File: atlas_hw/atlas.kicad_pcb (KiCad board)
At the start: 4 copper layers, 140.3 x 99.9 mm, 180 parts, among them J1 USB_C_Receptacle_USB2.0, J10 PSP_LCD, J11 UART3_EXT, J12 IO_EXT, J13 IO_MAIN, J2 DEBUG_STM, J3 PSP_TOUCH, J4 UPDI_DSS, J5 CELL_THERM, J6 LPM027M128B, J7 FLEX_12380-03, J8 Micro_SD_Card_Det, J9 PSP_LCD_BL, Q1 Q_NMOS_DGS, Q2 Q_NMOS_DGS, Q4 Q_NMOS_DGS, Q5 Q_NMOS_DGS, SW1 BTN_L_EXT, SW2 BTN_0_EXT, SW3 ResetSTM, SW4 BTN_R_EXT, SW5 BTN_PWR_EXT, U1 STM32H723VITx, U10 BQ25611D, U11 L96-M33, U13 LSF0108, U14 NPP600SNADJ, U15 TPS61073, U16 PAM2841, U2 S27KL0641DABHV023, U3 MCP1811B, U4 TLV62569DBV, U5 MX25L3233FM2I-08G, U6 LC709203F, U7 ATtiny402-SS, U8 MS5637, U9 MC6470, Y1 16M, Y4 32k

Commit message: passive placement
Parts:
- removed C55: 0.1u, Capacitor_SMD:C_0402_1005Metric
- removed R2, R80, R81: 0, Resistor_SMD:R_0402_1005Metric
- removed R46: 0, Resistor_SMD:R_0612_1632Metric
- added C20: 1u, Capacitor_SMD:C_0603_1608Metric, B.Cu at (206.1, 107.2)
- added C28: 0.1u, Capacitor_SMD:C_0402_1005Metric, B.Cu at (211.5, 112.5)
- C18, C19, C21, C22, C26, C5, C51, C53, C54, C56, C57, C6, C61, C9, R12, R13, R14, R15, R21, R22, R23, R26, R27, R30, R31, R32, R33, R35, R36, R39, R41, R82, R83, R84, R86: moved to B.Cu
- J11: footprint Connector_PinHeader_1.00mm:PinHeader_1x06_P1.00mm_Vertical -> Connector_PinHeader_1.00mm:PinHeader_1x06_P1.00mm_Vertical_SMD_Pin1Left
- J7, R37: moved to F.Cu
- R1, R25: value 10k -> 100k
- R44, R6: value 10k -> 100k; moved to B.Cu
- moved C51 242.5 mm to (208.6, 89.8), turned to 90 degrees
- moved C9 234.7 mm to (182.3, 94.4), turned to 90 degrees
- moved R86 224.2 mm to (214.2, 112.5), turned to 90 degrees
- moved C21 219.2 mm to (186.4, 107.0), turned to 45 degrees
- moved R55 214.3 mm to (195.3, 102.9), turned to 180 degrees
- moved C19 209.6 mm to (185.1, 108.3), turned to 225 degrees
- moved R82 209.0 mm to (206.8, 86.9), turned to 270 degrees
- moved R30 207.3 mm to (202.6, 130.3)
- moved C54 204.2 mm to (206.6, 106.0)
- moved C57 199.9 mm to (183.2, 127.3), turned to 90 degrees
- moved C2 196.7 mm to (190.0, 93.8), turned to 180 degrees
- moved R23 196.3 mm to (202.6, 133.3)
- moved R6 195.5 mm to (212.8, 112.5), turned to 90 degrees
- moved C27 195.3 mm to (205.8, 133.7), turned to 270 degrees
- moved R83 193.4 mm to (205.8, 86.9), turned to 270 degrees
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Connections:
- C48 pad 2: Net-(C48-Pad2) -> /VCC_SYS
- C51 pad 1: Net-(C51-Pad1) -> /VCC_LCD_PWR
- C53 pad 1: Net-(C51-Pad1) -> /VCC_LCD_PWR
- C54 pad 1: Net-(C54-Pad1) -> /VCC_MCU_3V3
- J10 pad 3: Net-(C54-Pad1) -> /VCC_MCU_3V3
- J10 pad 35: Net-(C51-Pad1) -> /VCC_LCD_PWR
- J10 pad 36: Net-(C51-Pad1) -> /VCC_LCD_PWR
- J10 pad 4: Net-(C54-Pad1) -> /VCC_MCU_3V3
- J11 pad 3: /USART3_RX_NCP -> /USART3_CTS_NCP
- J11 pad 4: /USART3_TX_NCP -> /USART3_RTS_NCP
- J11 pad 5: /USART3_CTS_NCP -> /USART3_TX_NCP
- J11 pad 6: /USART3_RTS_NCP -> /USART3_RX_NCP
- L10 pad 1: Net-(C48-Pad2) -> /VCC_SYS
- R1 pad 1: /VCC_BACKUP -> /VCC_MCU_3V3
- U1 pad 19: Net-(R2-Pad1) -> GND
- U13 pad 1: /VDD_SD_IO_3V3_1V8 -> GND
- U13 pad 10: /SDMMC1_D1 -> GND
- U13 pad 11: /SD_D1 -> GND
- U13 pad 12: /SD_D0 -> /SD_D2
- U13 pad 13: /SD_CLK -> /SD_D3
- U13 pad 14: /SD_CLK -> /SD_CMD
- U13 pad 15: /SD_CMD -> /SD_CLK
- U13 pad 16: /SD_D3 -> /SD_CLK
- U13 pad 17: /SD_D2 -> /SD_D0
- U13 pad 18: GND -> /SD_D1
- U13 pad 19: GND -> /VDD_SD_IO_3V3_1V8
- U13 pad 2: Net-(R43-Pad2) -> /VCC_MCU_3V3
- U13 pad 20: /VCC_MCU_3V3 -> Net-(R43-Pad2)
- U13 pad 21: /VDD_SD_IO_3V3_1V8 -> GND
- U13 pad 3: GND -> /SDMMC1_D1
- U13 pad 4: /SDMMC1_D2 -> /SDMMC1_D0
- U13 pad 5: /SDMMC1_D3 -> /SDMMC1_CKIN
- U13 pad 6: /SDMMC1_CMD -> /SDMMC1_CK
- U13 pad 7: /SDMMC1_CK -> /SDMMC1_CMD
- U13 pad 8: /SDMMC1_CKIN -> /SDMMC1_D3
- U13 pad 9: /SDMMC1_D0 -> /SDMMC1_D2
- U16 pad 2: Net-(C48-Pad2) -> /VCC_SYS
- U9 pad 10: (no net) -> Net-(U9-Pad10)
- Y1 pad 1: /RCC_OSC_IN -> /RCC_OSC_OUT
- Y1 pad 2: /RCC_OSC_OUT -> /RCC_OSC_IN
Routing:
- net /LTDC_VS: track 36.7 -> 4.70 mm
- net GND: track 34.9 -> 19.7 mm, vias 1 -> 0
- net /USB_PORT_VBUS: track 0.75 -> 16.0 mm
- net /GPS_3DF: track 0.00 -> 12.5 mm, vias 0 -> 1
- net /USART3_RTS_NCP: track 0.00 -> 12.0 mm
- net /USART3_RX_NCP: track 0.00 -> 11.4 mm
- net /CHG_STAT: track 1.21 -> 12.4 mm, vias 1 -> 2
- net /USART3_CTS_NCP: track 0.00 -> 10.7 mm
- net /SDMMC1_D1: track 0.00 -> 10.7 mm, vias 0 -> 1
- net /USART3_TX_NCP: track 0.00 -> 9.62 mm
- net /SDMMC1_D2: track 14.4 -> 5.60 mm, vias 1 -> 0
- net Net-(C48-Pad2): track 6.68 -> 0.00 mm
- net /VCC_SYS: track 7.19 -> 13.9 mm
- net /SDMMC1_D3: track 11.7 -> 5.08 mm
- net /SDMMC1_CKIN: track 5.08 -> 11.7 mm
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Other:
- board size 140.3 x 99.9 mm -> 60.5 x 77.4 mm

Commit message: filling out layout
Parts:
- removed R23, R30: 0, Resistor_SMD:R_0402_1005Metric
- C58: moved to B.Cu
- moved D2 52.6 mm to (182.0, 86.8)
- moved R10 49.6 mm to (182.0, 89.9)
- moved R36 7.59 mm to (196.6, 124.6)
- moved C58 1.41 mm to (177.6, 125.0), turned to 90 degrees
- moved R1 1.04 mm to (190.4, 125.2), turned to 45 degrees
- moved R49 0.96 mm to (196.1, 121.1), turned to 180 degrees
- moved R12 0.80 mm to (207.1, 133.0)
- moved R34 0.50 mm to (192.9, 103.9)
- moved C57 0.40 mm to (183.6, 127.3)
- moved C8 0.17 mm to (210.5, 109.7)
- moved R38 0.10 mm to (195.2, 103.9)
- moved R55 0.10 mm to (195.2, 102.9)
- moved C34 0.10 mm to (192.9, 102.9)
- moved J7 0.08 mm to (196.6, 122.8)
- turned R9 to 90 degrees
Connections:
- J13 pad 2: /SW_L -> /STM_STATUS_L
- J13 pad 3: /STM_STATUS_L -> /STM_STATUS_0
- J13 pad 4: /SW_0 -> /STM_STATUS_R
- J13 pad 5: /STM_STATUS_0 -> /SW_PWR
- J13 pad 7: /STM_STATUS_R -> /SW_0
- J13 pad 8: /SW_PWR -> /SW_L
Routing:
- net /VCC_BACKUP: track 0.00 -> 81.6 mm, vias 0 -> 5
- net /VCC_SYS: track 13.9 -> 88.1 mm, vias 0 -> 6
- net /VCC_MCU_3V3: track 7.54 -> 77.4 mm, vias 0 -> 20
- net GND: track 19.7 -> 77.9 mm, vias 0 -> 54
- net /SW_PWR: track 0.00 -> 44.6 mm, vias 0 -> 1
- net /USB_PORT_VBUS: track 16.0 -> 56.6 mm, vias 0 -> 2
- net /I2C4_SDA_SYSTEM: track 1.31 -> 40.8 mm, vias 1 -> 3
- net /PWR_ACK_DSS: track 0.00 -> 37.3 mm, vias 0 -> 2
- net /I2C4_SCL_SYSTEM: track 1.25 -> 37.4 mm, vias 1 -> 3
- net /PWR_SW_DSS: track 0.00 -> 35.3 mm, vias 0 -> 2
- net /DEBUG_SWDIO_STM: track 0.00 -> 31.2 mm, vias 0 -> 2
- net /DEBUG_SWDCLK_STM: track 0.00 -> 29.6 mm, vias 0 -> 2
- net /USB_STM_D+: track 0.00 -> 29.5 mm, vias 0 -> 1
- net /T3C1_LCD_BL: track 0.00 -> 27.9 mm, vias 0 -> 3
- net /USB_STM_D-: track 0.00 -> 27.5 mm, vias 0 -> 1
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- added copper zone on In1.Cu, net /VCC_MCU_3V3
- added copper zone on B.Cu, net GND
- added copper zone on F.Cu, net GND
- added copper zone on In2.Cu, net GND

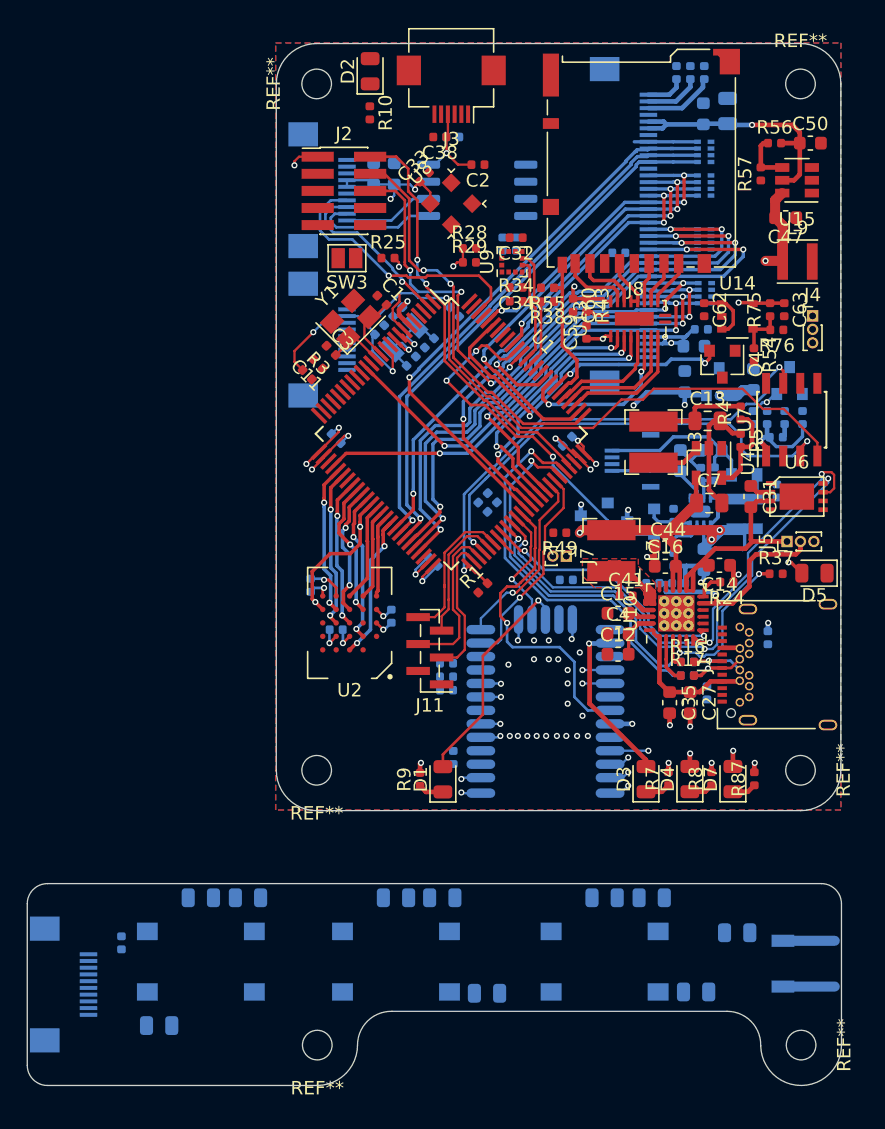
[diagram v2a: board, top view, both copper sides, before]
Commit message: layout mostly done, split btn into diffrent file
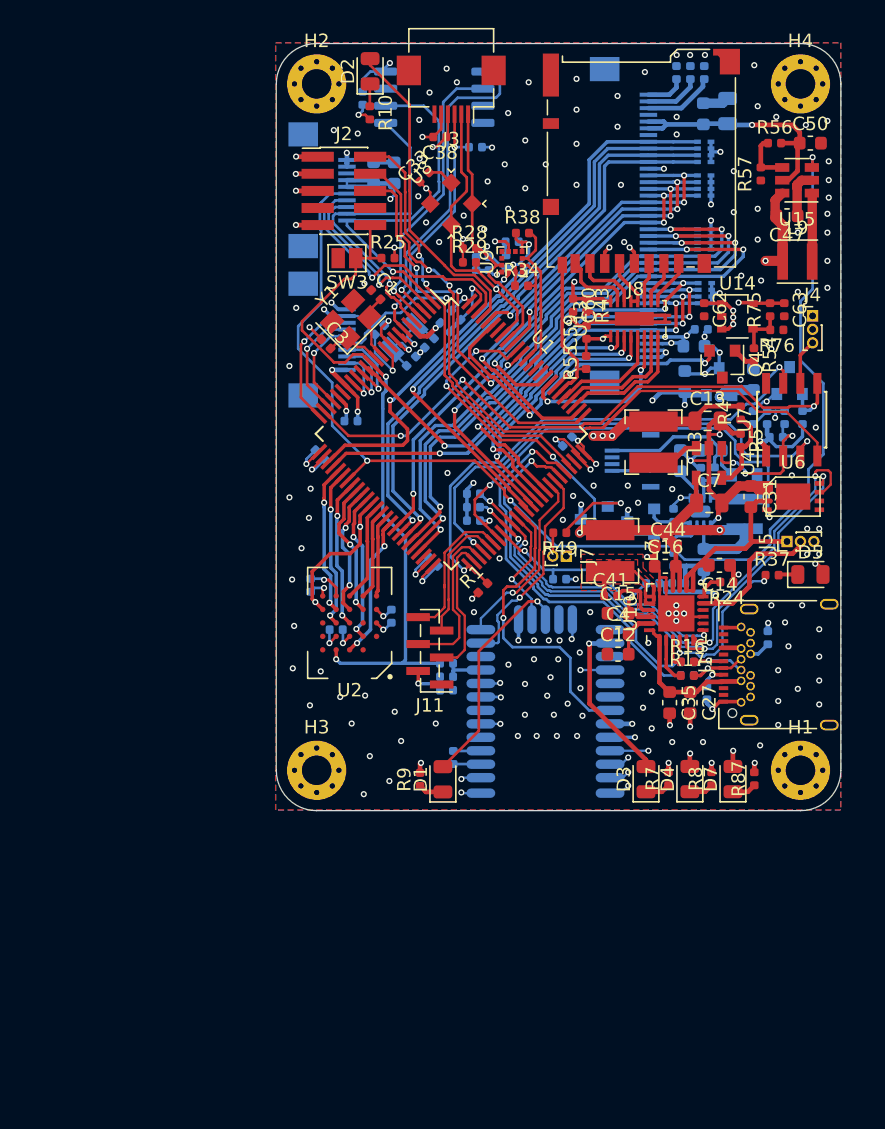
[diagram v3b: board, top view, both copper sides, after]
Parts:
- removed C17, C61: 0.1u, Capacitor_SMD:C_0402_1005Metric
- removed D10: STM_STATUS_R, LED_SMD:LED_0805_2012Metric
- removed D8: STM_STATUS_L, LED_SMD:LED_0805_2012Metric
- removed D9: STM_STATUS_0, LED_SMD:LED_0805_2012Metric
- removed J12: IO_EXT, Connector_FFC-FPC:Hirose_FH12-10S-0.5SH_1x10-1MP_P0.50mm_Horizontal
- removed R11, R18, R19: 1k, Resistor_SMD:R_0805_2012Metric
- removed R3: 0, Resistor_SMD:R_0402_1005Metric
- removed R40, R45, R48, R50: 100k, Resistor_SMD:R_0805_2012Metric
- removed REF** (x6): MountingHole_2.2mm_M2, MountingHole:MountingHole_2.2mm_M2
- removed SW1: BTN_L_EXT, Button_Switch_SMD:SW_SPST_B3S-1000
- removed SW2: BTN_0_EXT, Button_Switch_SMD:SW_SPST_B3S-1000
- removed SW4: BTN_R_EXT, Button_Switch_SMD:SW_SPST_B3S-1000
- removed SW5: BTN_PWR_EXT, Button_Switch_SMD:SW_SPST_B3U-1000P
- added H1: MountingHole_Pad, MountingHole:MountingHole_2.2mm_M2_Pad_Via, F.Cu at (214.0, 138.8)
- added H2: MountingHole_Pad, MountingHole:MountingHole_2.2mm_M2_Pad_Via, F.Cu at (178.1, 87.8)
- added H3: MountingHole_Pad, MountingHole:MountingHole_2.2mm_M2_Pad_Via, F.Cu at (178.1, 138.8)
- added H4: MountingHole_Pad, MountingHole:MountingHole_2.2mm_M2_Pad_Via, F.Cu at (214.0, 87.8)
- C11, C2, C32, C34: moved to B.Cu
- U10: footprint Package_DFN_QFN:WQFN-24-1EP_4x4mm_P0.5mm_EP2.7x2.7mm_ThermalVias -> Package_DFN_QFN:WQFN-24-1EP_4x4mm_P0.5mm_EP2.7x2.7mm
- moved R41 22.7 mm to (189.7, 120.2), turned to 0 degrees
- moved C2 9.89 mm to (181.5, 88.8), turned to 90 degrees
- moved U5 7.61 mm to (186.8, 88.7)
- moved R55 6.25 mm to (198.1, 108.5), turned to 90 degrees
- moved R38 5.43 mm to (193.3, 98.8), turned to 0 degrees
- moved C11 4.90 mm to (180.6, 112.8), turned to 0 degrees
- moved C6 3.70 mm to (187.6, 105.8), turned to 315 degrees
- moved R26 3.31 mm to (189.9, 101.1)
- moved C34 2.04 mm to (192.1, 101.0), turned to 90 degrees
- moved R42 1.85 mm to (189.8, 92.5), turned to 180 degrees
- moved R27 1.78 mm to (190.8, 101.1)
- moved C24 1.70 mm to (178.3, 115.3)
- moved R35 1.57 mm to (189.7, 119.2), turned to 0 degrees
- moved R33 1.22 mm to (189.7, 118.2), turned to 0 degrees
- moved R34 1.22 mm to (193.3, 102.8)
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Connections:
- C11 pad 1: Net-(C11-Pad1) -> /VCC_MCU_3V3
- R35 pad 2: /I2C4_SDA_SYSTEM -> /I2C4_SCL_SYSTEM
- U1 pad 16: /STM_STATUS_L -> /STM_STATUS_R
- U1 pad 18: /STM_STATUS_R -> /STM_STATUS_L
- U1 pad 21: Net-(C11-Pad1) -> /VCC_MCU_3V3
- U1 pad 22: /SW_C -> /SW_R
- U1 pad 23: /SW_L -> /SW_0
- U1 pad 25: /SW_R -> /SW_L
- U5 pad 1: /SPI4_FLASH_CS -> /SPI4_FLASH_NCS
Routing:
- net GND: track 77.9 -> 173.9 mm, vias 54 -> 197
- net /EN_LCD_PWR: track 3.40 -> 95.8 mm, vias 0 -> 3
- net /DEBUG_NRESET_STM: track 0.00 -> 50.6 mm, vias 0 -> 2
- net /~USB_DET: track 0.00 -> 46.5 mm, vias 0 -> 3
- net /LTDC_VS: track 4.70 -> 42.9 mm, vias 0 -> 1
- net /LC709203_INT: track 1.59 -> 35.7 mm, vias 0 -> 3
- net /SPI4_FLASH_NCS: track 0.00 -> 24.4 mm, vias 0 -> 1
- net /STM_STATUS_B: track 0.00 -> 23.9 mm
- net /I2C1_SDA_SENSOR: track 0.00 -> 23.4 mm, vias 0 -> 2
- net /SPI4_MISO_APP: track 0.00 -> 21.6 mm, vias 0 -> 1
- net /I2C1_SCL_SENSOR: track 0.00 -> 20.8 mm
- net /SPI4_SCK_APP: track 6.73 -> 26.5 mm, vias 0 -> 1
- net /VCC_MCU_3V3: track 77.4 -> 95.8 mm, vias 20 -> 40
- net /STC911_INT: track 3.24 -> 20.9 mm, vias 0 -> 2
- net /SPI4_MOSI_APP: track 9.40 -> 23.9 mm, vias 0 -> 1
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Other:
- board size 60.5 x 77.4 mm -> 41.9 x 57 mm

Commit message: atlas dev simplifcations
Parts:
- removed C31, C35, C47, C50: 1u, Capacitor_SMD:C_0603_1608Metric
- removed C33: 0.1u, Capacitor_SMD:C_0402_1005Metric
- removed C41: 47n, Capacitor_SMD:C_0402_1005Metric
- removed C44: 4.7u, Capacitor_SMD:C_0603_1608Metric
- removed D2: STM_STATUS_B, LED_SMD:LED_0805_2012Metric
- removed D5: CHARGE_STATUS, LED_SMD:LED_0805_2012Metric
- removed J11: UART3_EXT, Connector_PinHeader_1.00mm:PinHeader_1x06_P1.00mm_Vertical_SMD_Pin1Left
- removed J13: IO_MAIN, Connector_FFC-FPC:Hirose_FH12-10S-0.5SH_1x10-1MP_P0.50mm_Horizontal
- removed J7: FLEX_12380-03, Connector_PinHeader_1.00mm:PinHeader_1x02_P1.00mm_Vertical
- removed L7: 1u, Inductor_SMD:L_Bourns-SRN4018
- removed L9: L_Small, Inductor_SMD:L_Taiyo-Yuden_MD-3030
- removed Q5: Q_NMOS_DGS, Package_TO_SOT_SMD:SOT-23
- removed R33, R35: 4.7k, Resistor_SMD:R_0402_1005Metric
- removed R36, R41, R85, R86: 100k, Resistor_SMD:R_0402_1005Metric
- removed R37: 1k, Resistor_SMD:R_0402_1005Metric
- removed R49: 100, Resistor_SMD:R_0402_1005Metric
- removed R56, R57: NP, Resistor_SMD:R_0402_1005Metric
- removed U10: BQ25611D, Package_DFN_QFN:WQFN-24-1EP_4x4mm_P0.5mm_EP2.7x2.7mm
- removed U15: TPS61073, Package_TO_SOT_SMD:SOT-23-6
- removed U8: MS5637, atlas:QFN-4_3x3_Pitch2mm
- added C17: 0.1u, Capacitor_SMD:C_0402_1005Metric, F.Cu at (159.7, 112.0)
- added D10: STM_STATUS_R, LED_SMD:LED_0805_2012Metric, F.Cu at (150.8, 107.1)
- added D8: STM_STATUS_L, LED_SMD:LED_0805_2012Metric, F.Cu at (144.7, 112.6)
- added D9: STM_STATUS_0, LED_SMD:LED_0805_2012Metric, F.Cu at (139.5, 115.5)
- added L1: 2.2u, Inductor_SMD:L_Bourns-SRN4018, F.Cu at (145.5, 108.3)
- added R11: 1k, Resistor_SMD:R_0805_2012Metric, F.Cu at (153.5, 110.1)
- added R18: 1k, Resistor_SMD:R_0805_2012Metric, F.Cu at (148.3, 115.6)
- added R19: 1k, Resistor_SMD:R_0805_2012Metric, F.Cu at (164.6, 98.6)
- added R2: 100k, Resistor_SMD:R_0402_1005Metric, F.Cu at (156.8, 112.5)
- added R23: NP, Resistor_SMD:R_0402_1005Metric, F.Cu at (167.0, 108.0)
- added R3: 100k, Resistor_SMD:R_0402_1005Metric, F.Cu at (156.0, 115.0)
- added R30: NP, Resistor_SMD:R_0402_1005Metric, F.Cu at (162.6, 110.3)
- added R40: 100k, Resistor_SMD:R_0805_2012Metric, F.Cu at (155.7, 103.1)
- added R45: 100k, Resistor_SMD:R_0805_2012Metric, F.Cu at (160.2, 101.5)
- added R48: 100k, Resistor_SMD:R_0805_2012Metric, F.Cu at (155.2, 107.0)
- added R50: 100k, Resistor_SMD:R_0805_2012Metric, F.Cu at (149.1, 112.6)
- added SW1: BTN_L_EXT, Button_Switch_SMD:SW_SPST_B3S-1000, F.Cu at (148.0, 101.3)
- added SW2: BTN_0_EXT, Button_Switch_SMD:SW_SPST_B3S-1000, F.Cu at (136.9, 109.8)
- added SW4: BTN_R_EXT, Button_Switch_SMD:SW_SPST_B3S-1000, F.Cu at (136.9, 101.3)
- added SW5: BTN_PWR_EXT, Button_Switch_SMD:SW_SPST_B3U-1000P, F.Cu at (134.3, 116.2)
- C12, C14, C4: value 4.7u -> 1u
- C15: value 4.7u -> 10u; footprint Capacitor_SMD:C_0603_1608Metric -> Capacitor_SMD:C_0805_2012Metric
- C16: value 4.7u -> 0.1u; footprint Capacitor_SMD:C_0603_1608Metric -> Capacitor_SMD:C_0402_1005Metric
- C18: value 0.1u -> 10u; footprint Capacitor_SMD:C_0402_1005Metric -> Capacitor_SMD:C_0603_1608Metric; moved to F.Cu
- C5: value 0.1u -> 1u; moved to F.Cu
- C9: value 1u -> 10u; footprint Capacitor_SMD:C_0603_1608Metric -> Capacitor_SMD:C_0805_2012Metric; moved to F.Cu
- J1: value USB_C_Receptacle_USB2.0 -> USB_B_Micro; footprint Connector_USB:USB_C_Receptacle_Amphenol_12401548E4-2A -> Connector_USB:USB_Micro-B_Molex-105017-0001
- J5: value CELL_THERM -> EXP_L; footprint Connector_PinHeader_1.00mm:PinHeader_1x03_P1.00mm_Vertical -> Connector_PinHeader_2.54mm:PinHeader_1x18_P2.54mm_Vertical
- J6: value LPM027M128B -> EXP_R; footprint Connector_FFC-FPC:Hirose_FH12-10S-0.5SH_1x10-1MP_P0.50mm_Horizontal -> Connector_PinHeader_2.54mm:PinHeader_1x18_P2.54mm_Vertical; moved to F.Cu
- Q1: moved to F.Cu
- R10: value 1k -> 100k
- R12, R13: value 5.1k -> 0; moved to F.Cu
- R17, R24: value 0 -> NP
- R31, R32: value 100k -> NP; moved to F.Cu
- U6: value LC709203F -> ST1PS02; footprint atlas:WDFN-8_3x4mm_0.6mm_1.96x2.56mm -> atlas:TQFN-12_1.7x2.0mm_P0.4mm
- moved R13 56.8 mm to (156.0, 117.0), turned to 0 degrees
- moved C14 56.0 mm to (152.6, 115.3), turned to 0 degrees
- moved U6 55.2 mm to (159.9, 105.2), turned to 0 degrees
- moved J6 53.1 mm to (231.5, 92.6), turned to 0 degrees
- moved R12 52.1 mm to (161.2, 108.3), turned to 0 degrees
- moved C15 49.3 mm to (160.2, 98.6)
- moved R17 49.1 mm to (158.9, 116.5)
- moved Q1 47.7 mm to (155.8, 99.4), turned to 0 degrees
- moved R24 47.6 mm to (162.6, 112.3), turned to 0 degrees
- moved C4 46.7 mm to (157.8, 109.8)
- moved C12 46.2 mm to (164.4, 101.3)
- moved J1 45.4 mm to (238.8, 93.2), turned to 0 degrees
- moved R31 45.3 mm to (158.9, 114.5)
- moved R16 45.1 mm to (165.5, 110.0)
- moved R32 44.2 mm to (164.1, 108.0)
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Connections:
- C11 pad 1: /VCC_MCU_3V3 -> /VCC_3V3
- C12 pad 1: GND -> /VCAP2_STM
- C12 pad 2: Net-(C12-Pad2) -> GND
- C13 pad 1: /VCC_MCU_3V3 -> /VCC_3V3
- C14 pad 1: GND -> /VCAP2_STM
- C14 pad 2: /CELL_POS -> GND
- C15 pad 1: GND -> /VCC_CORE
- C15 pad 2: Net-(C15-Pad2) -> GND
- C16 pad 1: GND -> /VCAP2
- C16 pad 2: /VCC_SYS -> GND
- C18 pad 1: /VCC_MCU_3V3 -> /USB_PORT_VBUS
- C2 pad 2: /VCC_MCU_3V3 -> /VCC_3V3
- C22 pad 1: /VCC_MCU_3V3 -> /VCC_3V3
- C23 pad 1: /VCC_MCU_3V3 -> /VCC_3V3
- C24 pad 1: /VCC_MCU_3V3 -> /VCC_3V3
- C25 pad 1: /VCC_MCU_3V3 -> /VCC_3V3
- C26 pad 1: /VCC_MCU_3V3 -> /VCC_3V3
- C32 pad 1: /VCC_MCU_3V3 -> /VCC_3V3
- C34 pad 1: /VCC_MCU_3V3 -> /VCC_3V3
- C4 pad 1: GND -> /VCAP1_STM
- C4 pad 2: Net-(C12-Pad2) -> GND
- C5 pad 1: /VCC_MCU_3V3 -> /VCAP1_STM
- C51 pad 1: /VCC_LCD_PWR -> /VCC_SYS
- C53 pad 1: /VCC_LCD_PWR -> /VCC_SYS
- C56 pad 2: /VCC_MCU_3V3 -> /VCC_3V3
- C57 pad 2: /VCC_MCU_3V3 -> /VCC_3V3
- C58 pad 2: /VCC_MCU_3V3 -> /VCC_3V3
- C9 pad 1: /VCC_MCU_3V3 -> /VCC_SYS
- D4 pad 2: /VCC_MCU_3V3 -> /VCC_3V3
- J10 pad 35: /VCC_LCD_PWR -> /VCC_SYS
- J10 pad 36: /VCC_LCD_PWR -> /VCC_SYS
- J2 pad 1: /VCC_MCU_3V3 -> /VCC_3V3
- J5 pad 1: /CELL_POS -> /USB_PORT_VBUS
- J5 pad 2: /CELL_NTC -> /VCC_SYS
- J5 pad 3: GND -> /VCC_BACKUP
- J6 pad 1: /SPI4_SCK_APP -> GND
- J6 pad 10: GND -> /PE0
- J6 pad 2: /SPI4_MOSI_APP -> /SDMMC1_CKIN_PB8
- J6 pad 3: /SPI4_OPT_LCD_NCS -> /PB7
- J6 pad 4: /OPT_LCD_COM_INV -> /PB6
- J6 pad 5: /EN_LCD_PWR -> GND
- J6 pad 6: /VCC_MCU_3V3 -> /PD7
- J6 pad 7: /VCC_MCU_3V3 -> /PD6
- J6 pad 8: /EXTMODE -> /SDMMC1_VSEL_PD1
- J8 pad 9: /SDMMC1_DET -> /SD_DET
- L3 pad 2: /VCC_MCU_3V3 -> /VCC_3V3
- Q1 pad 1: Net-(Q1-Pad1) -> /VCORE_EN
- Q1 pad 2: /T3C1_LCD_BL -> /STM_VCORE_EN
- R10 pad 1: Net-(D2-Pad1) -> /STM_VCORE_GOOD
- R10 pad 2: GND -> /VCC_MCU_3V3
- R12 pad 1: GND -> /VCAP1
- R12 pad 2: Net-(J1-PadA5) -> /VCC_CORE
- R13 pad 1: Net-(J1-PadB5) -> /VCAP2
- R13 pad 2: GND -> /VCC_CORE
- R14 pad 1: /USB_STM_D- -> /USB_STM_D+
- R14 pad 2: /USB_PORT_D- -> /USB_PORT_D+
- R15 pad 1: /USB_STM_D+ -> /USB_STM_D-
- R15 pad 2: /USB_PORT_D+ -> /USB_PORT_D-
- R16 pad 1: /USB_CHGR_D- -> /VCC_SYS
- R16 pad 2: /USB_PORT_D- -> /USB_PORT_VBUS
- R17 pad 1: /USB_CHGR_D+ -> /SDMMC1_D2
- R17 pad 2: /USB_PORT_D+ -> /SD_D2
- R24 pad 1: GND -> /SDMMC1_CMD
- R24 pad 2: Net-(R24-Pad2) -> /SD_CMD
- R25 pad 2: /VCC_MCU_3V3 -> /VCC_3V3
- R31 pad 1: Net-(C15-Pad2) -> /SDMMC1_D0
- R31 pad 2: /CELL_NTC -> /SD_D0
- R32 pad 1: /CELL_NTC -> /SDMMC1_D1
- R32 pad 2: GND -> /SD_D1
- R4 pad 2: /VCC_MCU_3V3 -> /VCC_3V3
- R55 pad 1: /SDMMC1_DET -> /SD_DET
- U1 pad 1: /SPI4_SCK_APP -> /SPI4_SCK_APP_PE2
- U1 pad 100: /VCC_MCU_3V3 -> /VCC_3V3
- U1 pad 11: /VCC_MCU_3V3 -> /VCC_3V3
- U1 pad 2: /SPI4_OPT_LCD_NCS -> /PWR_ACK_DSS
- U1 pad 21: /VCC_MCU_3V3 -> /VCC_3V3
- U1 pad 24: /~USB_DET -> /PA2
- U1 pad 27: /VCC_MCU_3V3 -> /VCC_3V3
- U1 pad 4: /SPI4_MISO_APP -> /SPI4_MISO_APP_PE5
- U1 pad 48: Net-(U1-Pad48) -> /VCAP1_STM
- U1 pad 5: /SPI4_MOSI_APP -> /SPI4_MOSI_APP_PE6
- U1 pad 50: /VCC_MCU_3V3 -> /VCC_3V3
- U1 pad 51: /PWR_ACK_DSS -> /STM_VCORE_EN_PB12
- U1 pad 52: /USART3_CTS_NCP -> /STM_VCORE_D2_PB13
- U1 pad 53: /USART3_RTS_NCP -> /STM_VCORE_D1_PB14
- U1 pad 54: /PWR_SW_DSS -> /STM_VCORE_D0_PB15
- U1 pad 55: /USART3_TX_NCP -> /STM_VCORE_GOOD_PD8
- U1 pad 56: /USART3_RX_NCP -> /PD9
- U1 pad 57: /LC709203_INT -> /MC6470_INTM
- U1 pad 58: /BQ25611_INT -> /MC6470_INTA
- U1 pad 59: /I2C4_SCL_SYSTEM -> /I2C1_SCL_SENSOR
- U1 pad 60: /I2C4_SDA_SYSTEM -> /I2C1_SDA_SENSOR
- U1 pad 61: /GPS_FORCE_ON -> /STC911_INT
- U1 pad 62: /GPS_EXTINT -> /PD15
- U1 pad 7: /STC911_INT -> /PWR_SW_DSS
- U1 pad 73: Net-(U1-Pad73) -> /VCAP2_STM
- U1 pad 75: /VCC_MCU_3V3 -> /VCC_3V3
- U1 pad 82: /SDMMC1_VSEL -> /SDMMC1_VSEL_PD1
- U1 pad 85: Net-(U1-Pad85) -> /GPS_FORCE_ON
- U1 pad 86: Net-(U1-Pad86) -> /GPS_EXTINT
- U1 pad 87: /MC6470_INTM -> /PD6
- U1 pad 88: /MC6470_INTA -> /PD7
- U1 pad 92: /I2C1_SCL_SENSOR -> /PB6
- U1 pad 93: /I2C1_SDA_SENSOR -> /PB7
- U1 pad 95: /SDMMC1_CKIN -> /SDMMC1_CKIN_PB8
- U1 pad 97: /STM_STATUS_B -> /PE0
- U1 pad 98: /OPT_LCD_COM_INV -> /PE1
- U2 pad B4: /VCC_MCU_3V3 -> /VCC_3V3
- U2 pad D1: /VCC_MCU_3V3 -> /VCC_3V3
- U2 pad E4: /VCC_MCU_3V3 -> /VCC_3V3
- U5 pad 8: /VCC_MCU_3V3 -> /VCC_3V3
- U6 pad 1: GND -> Net-(R3-Pad2)
- U6 pad 2: GND -> /VCC_SYS
- U6 pad 3: /CELL_POS -> Net-(L1-Pad1)
- U6 pad 4: /LC709203_INT -> GND
- U6 pad 5: Net-(U6-Pad5) -> /VCC_CORE
- U6 pad 7: /I2C4_SDA_SYSTEM -> /STM_VCORE_GOOD
- U6 pad 8: /I2C4_SCL_SYSTEM -> Net-(R3-Pad2)
- U7 pad 5: /~USB_DET -> /DSS_EXT
- U9 pad 3: /VCC_MCU_3V3 -> /VCC_3V3
- U9 pad 7: /VCC_MCU_3V3 -> /VCC_3V3
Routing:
- net GND: track 173.9 -> 0.00 mm, vias 197 -> 0
- net /EN_LCD_PWR: track 95.8 -> 0.00 mm, vias 3 -> 0
- net /VCC_MCU_3V3: track 95.8 -> 0.00 mm, vias 40 -> 0
- net /VCC_SYS: track 91.0 -> 0.00 mm, vias 6 -> 0
- net /VCC_BACKUP: track 81.8 -> 0.00 mm, vias 5 -> 0
- net /USB_PORT_VBUS: track 57.5 -> 0.00 mm, vias 2 -> 0
- net /SW_PWR: track 53.8 -> 0.00 mm, vias 1 -> 0
- net /DEBUG_NRESET_STM: track 50.6 -> 0.00 mm, vias 2 -> 0
- net /LTDC_G5: track 48.5 -> 0.00 mm, vias 3 -> 0
- net /LTDC_G4: track 47.5 -> 0.00 mm, vias 3 -> 0
- net /~USB_DET: track 46.5 -> 0.00 mm, vias 3 -> 0
- net /I2C4_SDA_SYSTEM: track 43.8 -> 0.00 mm, vias 4 -> 0
- net /LTDC_G6: track 43.7 -> 0.00 mm, vias 3 -> 0
- net /LTDC_HS: track 43.2 -> 0.00 mm, vias 1 -> 0
- net /LTDC_VS: track 42.9 -> 0.00 mm, vias 1 -> 0
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- removed copper zone on In1.Cu, net /VCC_MCU_3V3
- removed copper zone on B.Cu, net GND
- removed copper zone on F.Cu, net GND
- removed copper zone on In2.Cu, net GND
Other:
- board outline removed
